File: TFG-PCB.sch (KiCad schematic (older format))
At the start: 25 parts, among them J1 TYPE-C-31-M-12, SW1 SW_Push, U1 ATmega32U4-AU, Y1 16MHz

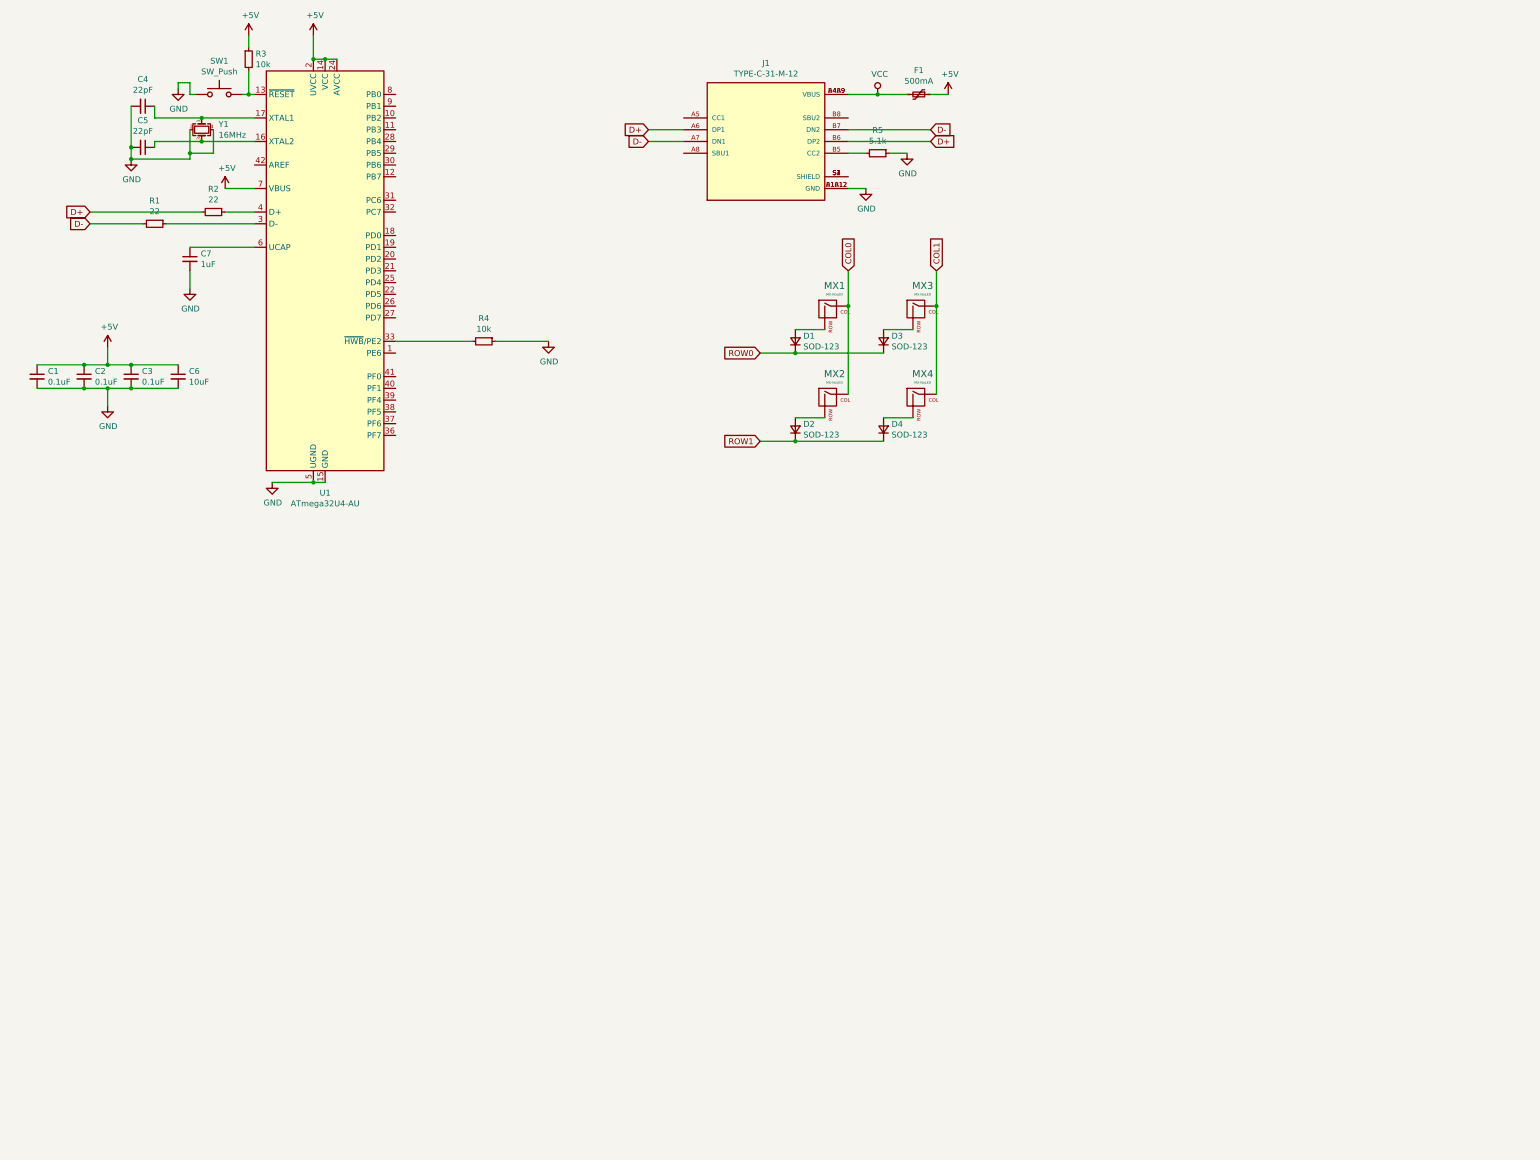
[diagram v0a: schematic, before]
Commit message: Added 60% keyboard schematics and started routing wires
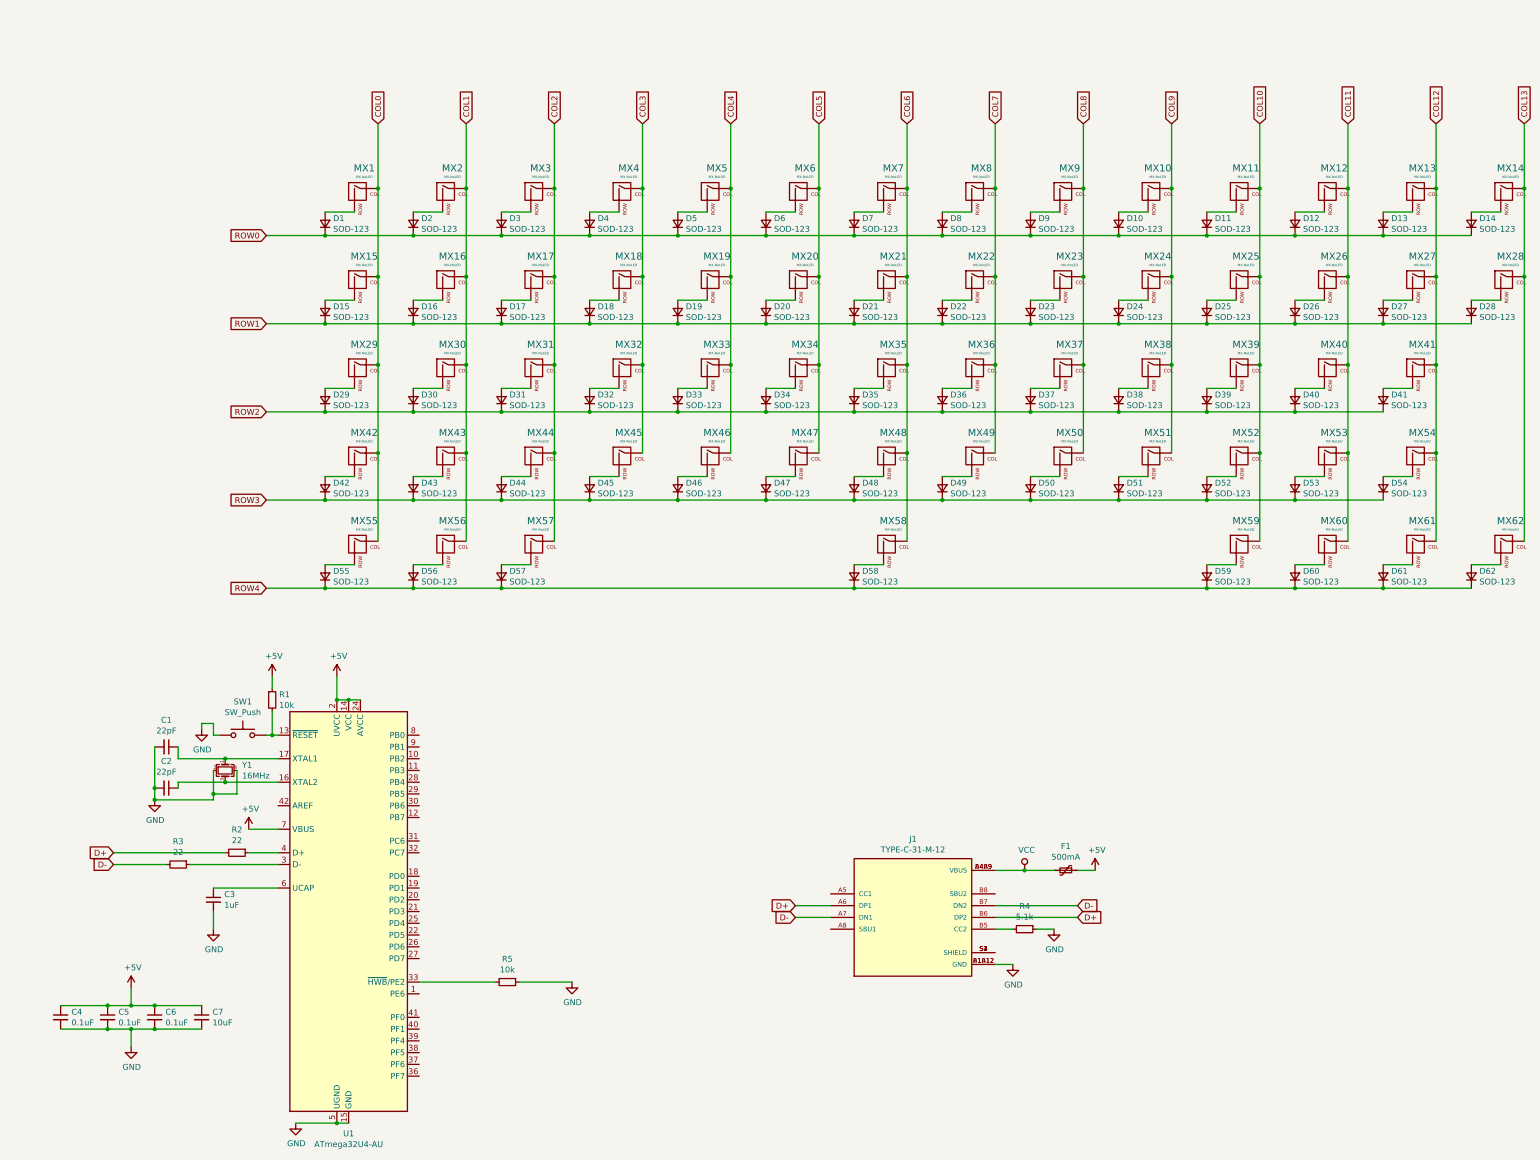
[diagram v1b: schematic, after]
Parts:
- added D10, D11, D12, D13, D14, D15, D16, D17, D18, D19, D20, D21, D22, D23, D24, D25, D26, D27, D28, D29, D30, D31, D32, D33, D34, D35, D36, D37, D38, D39, D40, D41, D42, D43, D44, D45, D46, D47, D48, D49, D5, D50, D51, D52, D53, D54, D55, D56, D57, D58, D59, D6, D60, D61, D62, D7, D8, D9: SOD-123, Diode_SMD:D_SOD-123, symbol Device:D_Small
- added MX10, MX11, MX12, MX13, MX16, MX17, MX18, MX19, MX20, MX21, MX22, MX23, MX24, MX25, MX26, MX27, MX30, MX31, MX32, MX33, MX34, MX35, MX36, MX37, MX38, MX39, MX40, MX41, MX43, MX44, MX45, MX46, MX47, MX48, MX49, MX5, MX50, MX51, MX52, MX53, MX6, MX7, MX8, MX9: MX-NoLED, MX_Only:MXOnly-1U, symbol MX_Alps_Hybrid:MX-NoLED
- added MX14: MX-NoLED, MX_Only:MXOnly-2U, symbol MX_Alps_Hybrid:MX-NoLED
- added MX15: MX-NoLED, MX_Only:MXOnly-1.5U, symbol MX_Alps_Hybrid:MX-NoLED
- added MX28: MX-NoLED, MX_Only:MXOnly-ISO, symbol MX_Alps_Hybrid:MX-NoLED
- added MX29: MX-NoLED, MX_Only:MXOnly-1.75U, symbol MX_Alps_Hybrid:MX-NoLED
- added MX42, MX55, MX56, MX57, MX59, MX60, MX61, MX62: MX-NoLED, MX_Only:MXOnly-1.25U, symbol MX_Alps_Hybrid:MX-NoLED
- added MX54: MX-NoLED, MX_Only:MXOnly-2.75U, symbol MX_Alps_Hybrid:MX-NoLED
- added MX58: MX-NoLED, MX_Only:MXOnly-6.25U, symbol MX_Alps_Hybrid:MX-NoLED
- renumbered C4 to C1, C5 to C2, C7 to C3, C1 to C4, C2 to C5, C3 to C6, C6 to C7, R3 to R1, R1 to R3, R5 to R4, R4 to R5
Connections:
- net COL0: now also MX15.1 (COL), MX29.1 (COL), MX42.1 (COL), MX55.1 (COL); no longer MX2.1 (COL)
- net COL1: now also MX2.1 (COL), MX16.1 (COL), MX30.1 (COL), MX43.1 (COL), MX56.1 (COL); no longer MX3.1 (COL), MX4.1 (COL)
- net ROW0: now also D2.1 (K), D4.1 (K), D10.1 (K), D11.1 (K), D12.1 (K), D13.1 (K), D14.1 (K), D5.1 (K), D6.1 (K), D7.1 (K), D8.1 (K), D9.1 (K)
- net ROW1: now also D15.1 (K), D16.1 (K), D17.1 (K), D18.1 (K), D19.1 (K), D20.1 (K), D21.1 (K), D22.1 (K), D23.1 (K), D24.1 (K), D25.1 (K), D26.1 (K), D27.1 (K), D28.1 (K); no longer D2.1 (K), D4.1 (K)
- new net: D18.2 (A), MX18.2 (ROW)
- new net: D5.2 (A), MX5.2 (ROW)
- new net: D19.2 (A), MX19.2 (ROW)
- new net: D6.2 (A), MX6.2 (ROW)
- new net: D20.2 (A), MX20.2 (ROW)
- new net: D7.2 (A), MX7.2 (ROW)
- new net: D21.2 (A), MX21.2 (ROW)
- new net: D8.2 (A), MX8.2 (ROW)
- new net: D22.2 (A), MX22.2 (ROW)
- new net: D9.2 (A), MX9.2 (ROW)
- new net: D23.2 (A), MX23.2 (ROW)
- new net: D10.2 (A), MX10.2 (ROW)
- new net: D24.2 (A), MX24.2 (ROW)
- new net: D11.2 (A), MX11.2 (ROW)
- new net: D25.2 (A), MX25.2 (ROW)
- new net: D30.2 (A), MX30.2 (ROW)
- new net: D43.2 (A), MX43.2 (ROW)
- new net: D31.2 (A), MX31.2 (ROW)
- new net: D44.2 (A), MX44.2 (ROW)
- new net: D32.2 (A), MX32.2 (ROW)
- new net: D45.2 (A), MX45.2 (ROW)
- new net: D33.2 (A), MX33.2 (ROW)
- new net: D46.2 (A), MX46.2 (ROW)
- new net: D34.2 (A), MX34.2 (ROW)
- new net: D47.2 (A), MX47.2 (ROW)
- new net: D35.2 (A), MX35.2 (ROW)
- new net: D48.2 (A), MX48.2 (ROW)
- new net: D36.2 (A), MX36.2 (ROW)
- new net: D49.2 (A), MX49.2 (ROW)
- new net: D37.2 (A), MX37.2 (ROW)
- new net: D50.2 (A), MX50.2 (ROW)
- new net: D38.2 (A), MX38.2 (ROW)
- new net: D51.2 (A), MX51.2 (ROW)
- new net: D39.2 (A), MX39.2 (ROW)
- new net: D52.2 (A), MX52.2 (ROW)
- new net: D16.2 (A), MX16.2 (ROW)
- new net: D17.2 (A), MX17.2 (ROW)
- new net: D12.2 (A), MX12.2 (ROW)
- new net: D26.2 (A), MX26.2 (ROW)
- new net: D40.2 (A), MX40.2 (ROW)
- new net: D53.2 (A), MX53.2 (ROW)
- new net: D29.2 (A), MX29.2 (ROW)
- new net: D42.2 (A), MX42.2 (ROW)
- new net: D15.2 (A), MX15.2 (ROW)
- new net: D13.2 (A), MX13.2 (ROW)
- new net: D27.2 (A), MX27.2 (ROW)
- new net: D41.2 (A), MX41.2 (ROW)
- new net: D54.2 (A), MX54.2 (ROW)
- new net: D14.2 (A), MX14.2 (ROW)
- new net: D28.2 (A), MX28.2 (ROW)
- new net: D56.2 (A), MX56.2 (ROW)
- new net: D57.2 (A), MX57.2 (ROW)
- new net: D58.2 (A), MX58.2 (ROW)
- new net: D59.2 (A), MX59.2 (ROW)
- new net: D60.2 (A), MX60.2 (ROW)
- new net: D55.2 (A), MX55.2 (ROW)
- new net: D61.2 (A), MX61.2 (ROW)
- new net: D62.2 (A), MX62.2 (ROW)
- new net COL10: MX11.1 (COL), MX25.1 (COL), MX39.1 (COL), MX52.1 (COL), MX59.1 (COL)
- new net COL11: MX12.1 (COL), MX26.1 (COL), MX40.1 (COL), MX53.1 (COL), MX60.1 (COL)
- new net COL12: MX13.1 (COL), MX27.1 (COL), MX41.1 (COL), MX54.1 (COL), MX61.1 (COL)
- new net COL13: MX14.1 (COL), MX28.1 (COL), MX62.1 (COL)
- new net COL2: MX17.1 (COL), MX3.1 (COL), MX31.1 (COL), MX44.1 (COL), MX57.1 (COL)
- new net COL3: MX18.1 (COL), MX32.1 (COL), MX4.1 (COL), MX45.1 (COL)
- new net COL4: MX19.1 (COL), MX33.1 (COL), MX46.1 (COL), MX5.1 (COL)
- new net COL5: MX20.1 (COL), MX34.1 (COL), MX47.1 (COL), MX6.1 (COL)
- new net COL6: MX21.1 (COL), MX35.1 (COL), MX48.1 (COL), MX58.1 (COL), MX7.1 (COL)
- new net COL7: MX22.1 (COL), MX36.1 (COL), MX49.1 (COL), MX8.1 (COL)
- new net COL8: MX23.1 (COL), MX37.1 (COL), MX50.1 (COL), MX9.1 (COL)
- new net COL9: MX10.1 (COL), MX24.1 (COL), MX38.1 (COL), MX51.1 (COL)
- new net ROW2: D29.1 (K), D30.1 (K), D31.1 (K), D32.1 (K), D33.1 (K), D34.1 (K), D35.1 (K), D36.1 (K), D37.1 (K), D38.1 (K), D39.1 (K), D40.1 (K), D41.1 (K)
- new net ROW3: D42.1 (K), D43.1 (K), D44.1 (K), D45.1 (K), D46.1 (K), D47.1 (K), D48.1 (K), D49.1 (K), D50.1 (K), D51.1 (K), D52.1 (K), D53.1 (K), D54.1 (K)
- new net ROW4: D55.1 (K), D56.1 (K), D57.1 (K), D58.1 (K), D59.1 (K), D60.1 (K), D61.1 (K), D62.1 (K)
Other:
- moved on the sheet: C1, C2, C3, C4, C5, C6, C7, F1, J1, R1, R2, R3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

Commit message: Renamed Footprints to account for keys
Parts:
- MX1: value MX-NoLED -> Esc
- MX10: value MX-NoLED -> 9
- MX11: value MX-NoLED -> 0
- MX12: value MX-NoLED -> -
- MX13: value MX-NoLED -> =
- MX14: value MX-NoLED -> BkSpc
- MX15: value MX-NoLED -> Tab
- MX16: value MX-NoLED -> Q
- MX17: value MX-NoLED -> W
- MX18: value MX-NoLED -> E
- MX19: value MX-NoLED -> R
- MX2: value MX-NoLED -> 1
- MX20: value MX-NoLED -> T
- MX21: value MX-NoLED -> Y
- MX22: value MX-NoLED -> U
- MX23: value MX-NoLED -> I
- MX24: value MX-NoLED -> O
- MX25: value MX-NoLED -> P
- MX26: value MX-NoLED -> [
- MX27: value MX-NoLED -> ]
- MX28: value MX-NoLED -> Enter
- MX29: value MX-NoLED -> CapsLck
- MX3: value MX-NoLED -> 2
- MX30: value MX-NoLED -> A
- MX31: value MX-NoLED -> S
- MX32: value MX-NoLED -> D
- MX33: value MX-NoLED -> F
- MX34: value MX-NoLED -> G
- MX35: value MX-NoLED -> H
- MX36: value MX-NoLED -> J
- MX37: value MX-NoLED -> K
- MX38: value MX-NoLED -> L
- MX39: value MX-NoLED -> ;
- MX4: value MX-NoLED -> 3
- MX40: value MX-NoLED -> '
- MX41: value MX-NoLED -> #
- MX42: value MX-NoLED -> LShift
- MX43: value MX-NoLED -> \\
- MX44: value MX-NoLED -> Z
- MX45: value MX-NoLED -> X
- MX46: value MX-NoLED -> C
- MX47: value MX-NoLED -> V
- MX48: value MX-NoLED -> B
- MX49: value MX-NoLED -> N
- MX5: value MX-NoLED -> 4
- MX50: value MX-NoLED -> M
- MX51: value MX-NoLED -> ,
- MX52: value MX-NoLED -> .
- MX53: value MX-NoLED -> /
- MX54: value MX-NoLED -> RShift
- MX55: value MX-NoLED -> LCtrl
- MX56: value MX-NoLED -> LWin
- MX57: value MX-NoLED -> LAlt
- MX58: value MX-NoLED -> Space
- MX59: value MX-NoLED -> RAlt
- MX6: value MX-NoLED -> 5
- MX60: value MX-NoLED -> RWin
- MX61: value MX-NoLED -> RCtrl
- MX62: value MX-NoLED -> Fn
- MX7: value MX-NoLED -> 6
- MX8: value MX-NoLED -> 7
- MX9: value MX-NoLED -> 8
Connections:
- net CC1: now reaches J1.A5 (CC1)
- net CC1: now also J1.B5 (CC2), R4.2
- no-connect marks 0 -> 2

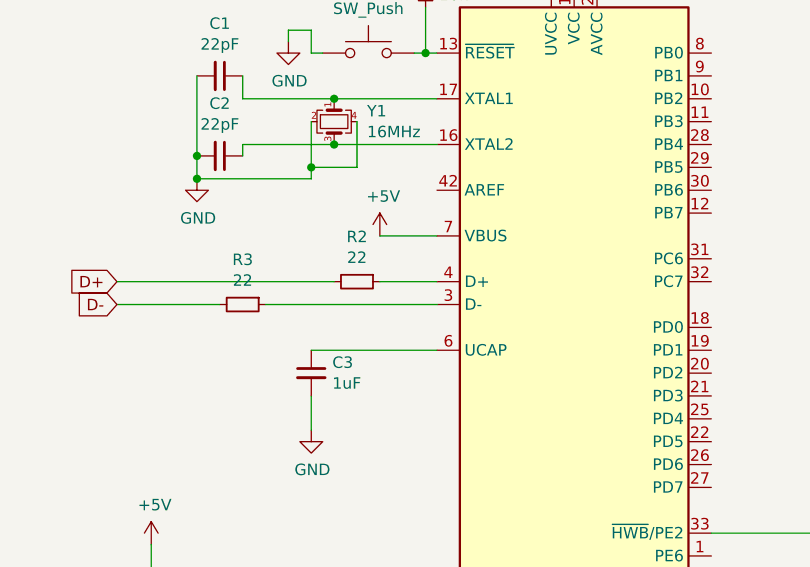
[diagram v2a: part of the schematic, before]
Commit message: Moved diodes + started wiring
Moved diodes (again) and started differential wiring
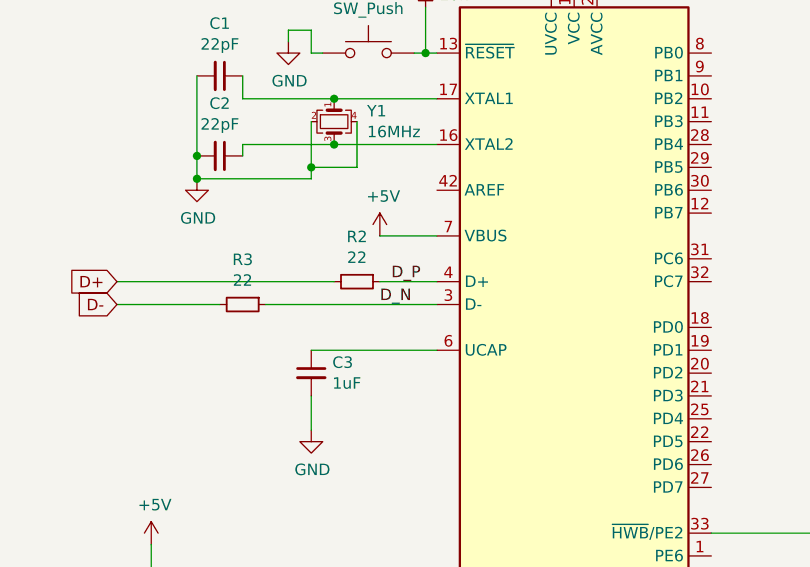
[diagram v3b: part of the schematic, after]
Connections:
- net D_N: now reaches R3.1, U1.3 (D-)
- net D_P: now reaches R2.1, U1.4 (D+)
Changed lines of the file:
@@
 NoConn ~ 9000 8350
 NoConn ~ 7600 8650
+Text Label 2700 8000 0    50   ~ 0
+D_P
+Text Label 2650 8100 0    50   ~ 0
+D_N
 $EndSCHEMATC

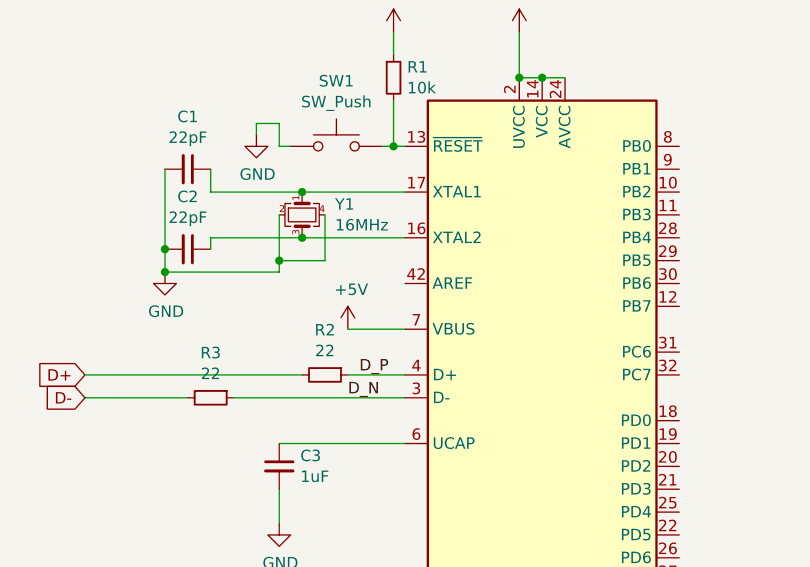
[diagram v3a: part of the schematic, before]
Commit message: Rewiring + moving diodes
Moved diodes (for the last time i think) and started wiring MC
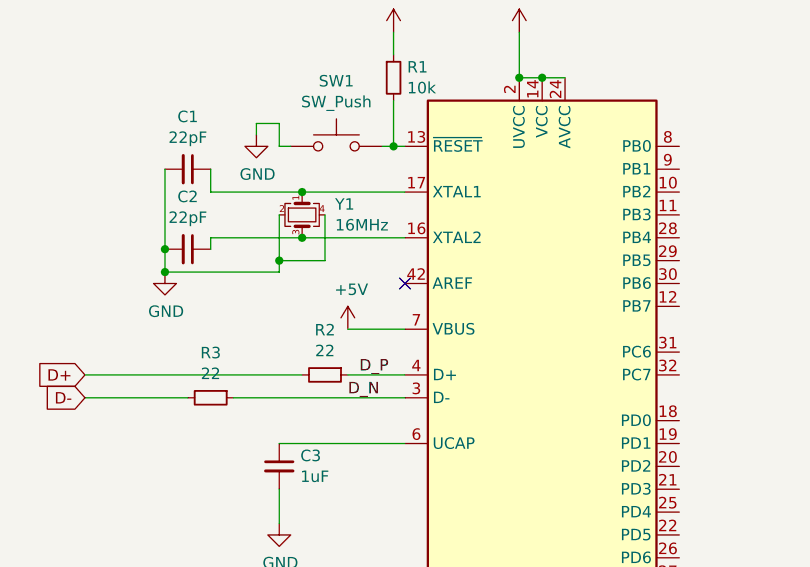
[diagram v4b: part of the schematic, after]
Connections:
- no-connect marks 2 -> 3
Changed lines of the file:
@@
 Text Label 2650 8100 0    50   ~ 0
 D_N
+NoConn ~ 2900 7600
 $EndSCHEMATC
